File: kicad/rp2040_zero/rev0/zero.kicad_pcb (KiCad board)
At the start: 2 copper layers, 41.8 x 30.2 mm, 23 parts, among them J1 jtag, J2 Conn_01x03_Socket, J5 Debug port, U1 RP2040-Zero, U3 3V->VTREF, U4 VTREF->3V, U5 VTREF<->3V, U6 RT9013-33GB

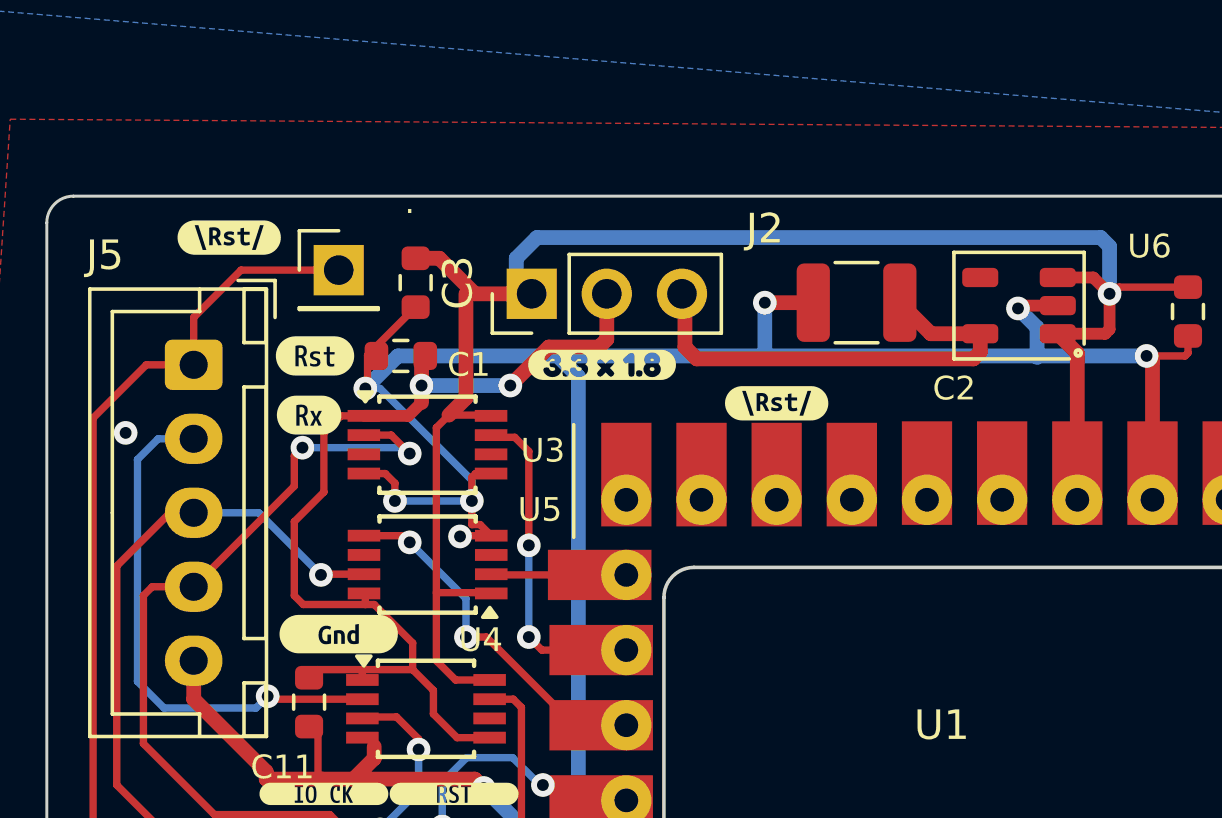
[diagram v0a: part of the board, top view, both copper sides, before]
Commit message: kicad: rp2040, simplify layout
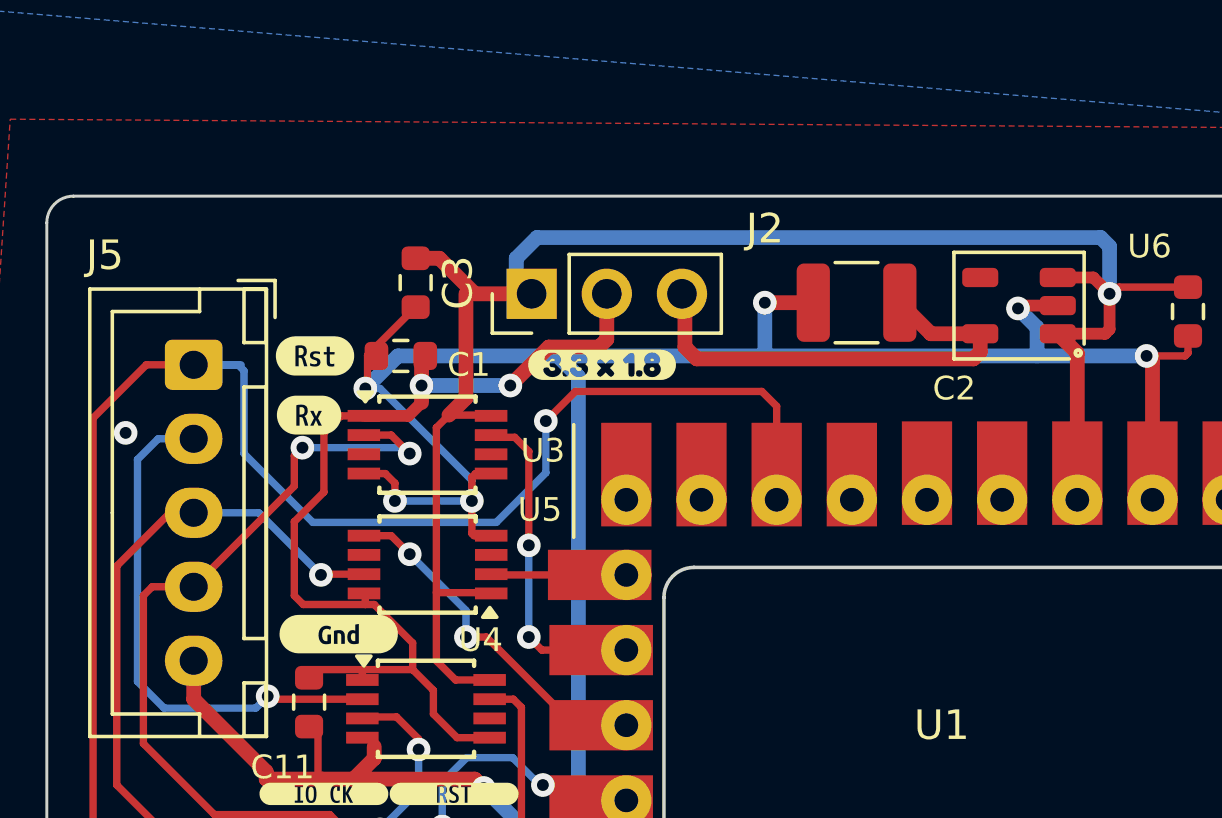
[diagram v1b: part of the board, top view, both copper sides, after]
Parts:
- removed .: PinHeader_1x01_P2.54mm_Vertical, Connector_PinHeader_2.54mm:PinHeader_1x01_P2.54mm_Vertical
- removed kibuzzard-6719D73B (x2): G***, kibuzzard-6719D73B
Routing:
- net INOUT_NRESET: track 52.8 -> 76.1 mm, vias 4 -> 5
- net GND: track 113.0 -> 112.1 mm, vias 11 -> 10
